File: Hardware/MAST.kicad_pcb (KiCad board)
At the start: 6 copper layers, 26 x 15 mm, 122 parts, among them J1 S+, J2 S-, J3 S-, J4 BAT+, J5 BAT-, Q1 DMP21D0UFB4, Q2 PMZ290UNE2, U1 LP5907SNX-3.0, U2 TPS62748, U3 ARTIC-R2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

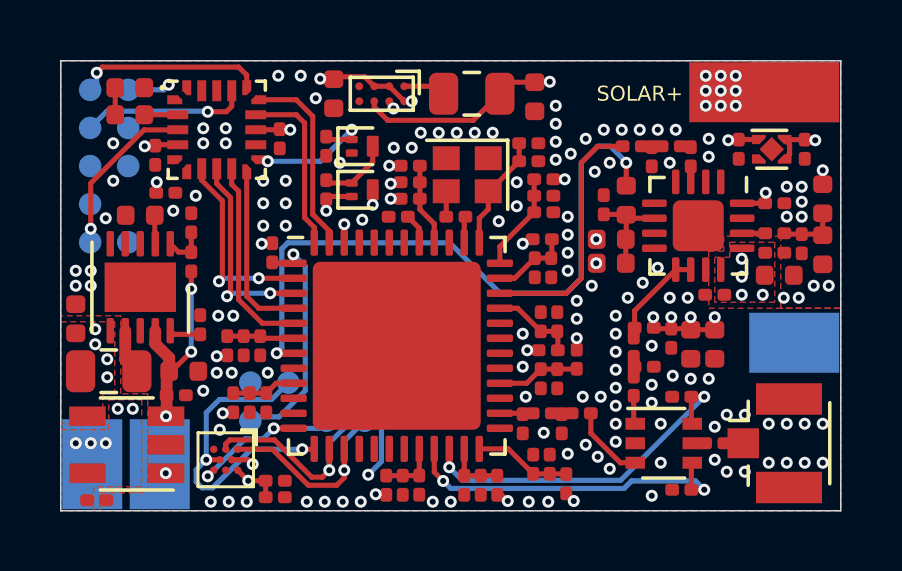
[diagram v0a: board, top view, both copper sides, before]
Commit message: Fix flash chip orientation
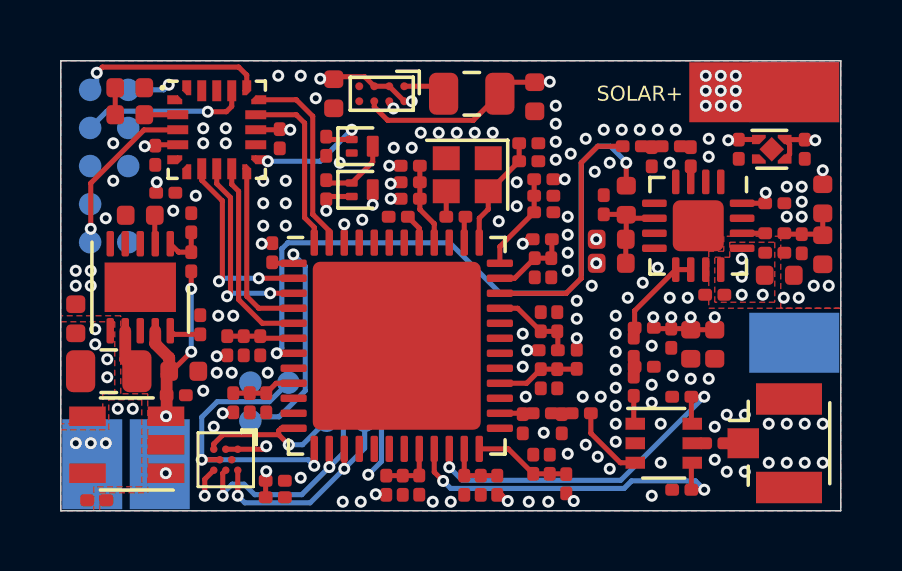
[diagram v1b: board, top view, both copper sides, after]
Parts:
- L1, L10, L2, L3, L4, L5, L6, L7, L8, L9: value 220@100MHz -> 120@100MHz
- R9: value 3.1M -> 3.09M
- X1: value 26MHz -> TCXO, 26MHz, <1ppm
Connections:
- U4 pad A1: FLASH_nEN -> ARTIC_3V3
- U4 pad A3: ARTIC_3V3 -> FLASH_nEN
- U4 pad C1: FLASH_MISO -> ARTIC_3V3
- U4 pad C3: Net-(U4-PadC3) -> FLASH_MISO
- U4 pad E1: Net-(U4-PadE1) -> FLASH_CLK
- U4 pad E3: FLASH_CLK -> ARTIC_3V3
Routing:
- net ARTIC_3V3: track 17.1 -> 18.7 mm, vias 16 -> 18
- net FLASH_MOSI: track 10.6 -> 9.78 mm
- net GND: track 1.74 -> 0.98 mm, vias 139 -> 134
- net FLASH_MISO: track 8.35 -> 9.02 mm, vias 1 -> 2
- net FLASH_CLK: track 5.67 -> 5.20 mm, vias 2 -> 1
- net FLASH_nEN: track 7.04 -> 7.51 mm, vias 1 -> 2

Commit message: Improve RF 1.8V & 3.3V rail power delivery
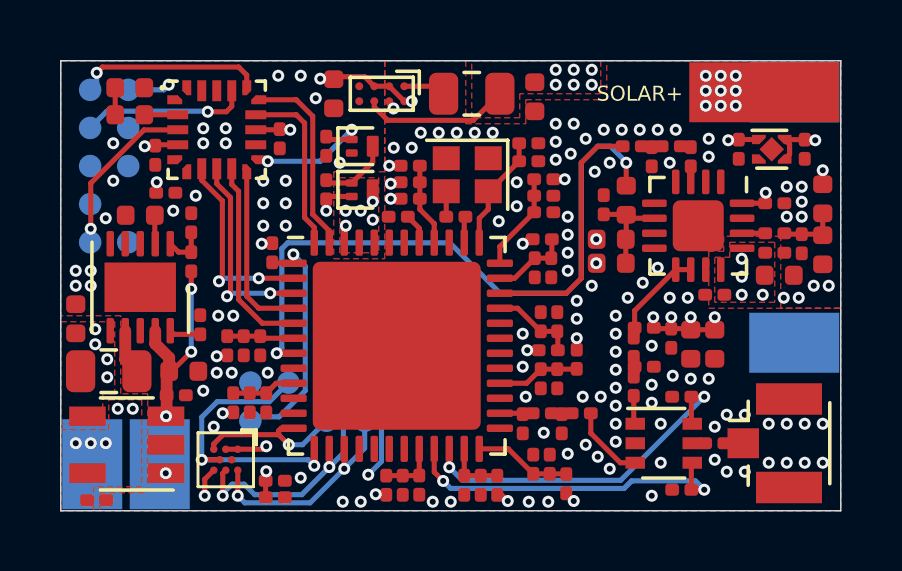
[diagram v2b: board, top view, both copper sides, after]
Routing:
- net ARTIC_1V8: track 9.37 -> 7.54 mm, vias 8 -> 13
- net ARTIC_3V3: track 18.7 -> 17.6 mm, vias 18 -> 21
- net GND: vias 134 -> 133
- added copper zone on F.Cu, net ARTIC_1V8
- added copper zone on F.Cu, net ARTIC_3V3
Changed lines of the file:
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@@
     (thickness 1.2)
     (drawings 12)
-    (tracks 574)
+    (tracks 575)
     (zones 0)
     (modules 122)
@@
   (via (at 207 45.6) (size 0.4) (drill 0.2) (layers F.Cu B.Cu) (net 1))
   (segment (start 207.33 45.6) (end 207 45.6) (width 0.171) (layer F.Cu) (net 1))
-  (via (at 206.05 46.3) (size 0.4) (drill 0.2) (layers F.Cu B.Cu) (net 1))
   (via (at 205.3 44.4) (size 0.4) (drill 0.2) (layers F.Cu B.Cu) (net 1))
   (via (at 201.7 51.4) (size 0.4) (drill 0.2) (layers F.Cu B.Cu) (net 1))
@@
   (segment (start 206.95 42.449772) (end 207.090137 42.589909) (width 0.171) (layer F.Cu) (net 1))
   (via (at 212.5 43.1) (size 0.4) (drill 0.2) (layers F.Cu B.Cu) (net 1))
-  (via (at 212.5 42.5) (size 0.4) (drill 0.2) (layers F.Cu B.Cu) (net 1))
   (via (at 202.75 45) (size 0.4) (drill 0.2) (layers F.Cu B.Cu) (net 1))
   (via (at 203.5 45) (size 0.4) (drill 0.2) (layers F.Cu B.Cu) (net 1))
@@
   (via (at 202.9 51.4) (size 0.4) (drill 0.2) (layers F.Cu B.Cu) (net 1))
   (via (at 201.1 53.2) (size 0.4) (drill 0.2) (layers F.Cu B.Cu) (net 1))
+  (via (at 213.1 43.1) (size 0.4) (drill 0.2) (layers F.Cu B.Cu) (net 1))
+  (via (at 206.4 45.7) (size 0.4) (drill 0.2) (layers F.Cu B.Cu) (net 9))
+  (via (at 205.5 46.5) (size 0.4) (drill 0.2) (layers F.Cu B.Cu) (net 9))
+  (via (at 206 46) (size 0.4) (drill 0.2) (layers F.Cu B.Cu) (net 9))
+  (via (at 205.5 46) (size 0.4) (drill 0.2) (layers F.Cu B.Cu) (net 9))
   (segment (start 218.75 53.75) (end 218.12 53.75) (width 0.171) (layer F.Cu) (net 2))
   (segment (start 212.57 50.04) (end 212.55 50.02) (width 0.171) (layer F.Cu) (net 3))
@@
   (via (at 212.8 44.95) (size 0.4) (drill 0.2) (layers F.Cu B.Cu) (net 9))
   (segment (start 212.42 44.95) (end 212.8 44.95) (width 0.171) (layer F.Cu) (net 9))
-  (via (at 205.45 46.45) (size 0.4) (drill 0.2) (layers F.Cu B.Cu) (net 9))
-  (segment (start 205.45 47.0625) (end 205.45 46.45) (width 0.171) (layer F.Cu) (net 9))
   (via (at 201.4 52.75) (size 0.4) (drill 0.2) (layers F.Cu B.Cu) (net 9))
   (segment (start 201.75 52.72) (end 201.43 52.72) (width 0.171) (layer F.Cu) (net 9))
@@
   (segment (start 206.13 51.73) (end 206.690501 52.290501) (width 0.171) (layer B.Cu) (net 9))
   (segment (start 206.690501 52.290501) (end 206.690501 54.359499) (width 0.171) (layer B.Cu) (net 9))
-  (via (at 206.4 45.8) (size 0.4) (drill 0.2) (layers F.Cu B.Cu) (net 9))
-  (segment (start 206.4 45.3) (end 206.4 45.8) (width 0.171) (layer F.Cu) (net 9))
   (via (at 210.9 55.675) (size 0.4) (drill 0.2) (layers F.Cu B.Cu) (net 9))
   (segment (start 210.55 55.47) (end 210.695 55.47) (width 0.171) (layer F.Cu) (net 9))
@@
   (via (at 202.85 54.6855) (size 0.4) (drill 0.2) (layers F.Cu B.Cu) (net 9))
   (segment (start 202.83 54.7055) (end 202.85 54.6855) (width 0.171) (layer F.Cu) (net 9))
+  (via (at 206.4 46.3) (size 0.4) (drill 0.2) (layers F.Cu B.Cu) (net 9))
   (via (at 218.25 43.65) (size 0.4) (drill 0.2) (layers F.Cu B.Cu) (net 10))
   (segment (start 218.6 43.63) (end 218.27 43.63) (width 0.171) (layer F.Cu) (net 10))
@@
   (segment (start 206.898127 42.98551) (end 206.45 42.537383) (width 0.171) (layer F.Cu) (net 15))
   (segment (start 210.6375 42.1) (end 209.75199 42.98551) (width 0.171) (layer F.Cu) (net 15))
-  (segment (start 211.0225 41.715) (end 210.6375 42.1) (width 0.171) (layer F.Cu) (net 15))
-  (segment (start 211.8 41.715) (end 211.0225 41.715) (width 0.171) (layer F.Cu) (net 15))
-  (segment (start 211.8 41.715) (end 212.285 41.715) (width 0.171) (layer F.Cu) (net 15))
-  (via (at 212.3 41.7) (size 0.4) (drill 0.2) (layers F.Cu B.Cu) (net 15))
-  (segment (start 212.285 41.715) (end 212.3 41.7) (width 0.171) (layer F.Cu) (net 15))
+  (via (at 212.5 41.8) (size 0.4) (drill 0.2) (layers F.Cu B.Cu) (net 15))
+  (via (at 212.5 41.3) (size 0.4) (drill 0.2) (layers F.Cu B.Cu) (net 15))
+  (via (at 213.1 41.3) (size 0.4) (drill 0.2) (layers F.Cu B.Cu) (net 15))
+  (via (at 213.1 41.8) (size 0.4) (drill 0.2) (layers F.Cu B.Cu) (net 15))
+  (via (at 213.7 41.8) (size 0.4) (drill 0.2) (layers F.Cu B.Cu) (net 15))
+  (via (at 213.7 41.3) (size 0.4) (drill 0.2) (layers F.Cu B.Cu) (net 15))
   (segment (start 211.28 43.75) (end 211.28 44.35) (width 0.171) (layer F.Cu) (net 16))
   (segment (start 210.28 45.35) (end 210.25 45.35) (width 0.171) (layer F.Cu) (net 16))
@@
       (pts
         (xy 197.3 56) (xy 197.3 55.4) (xy 198.9 55.4) (xy 198.9 52.1) (xy 198 52.1)
-        (xy 198 49.5) (xy 196 49.5) (xy 196 41) (xy 222 41) (xy 222 49.25)
-        (xy 220 49.25) (xy 220 46.85) (xy 218.1 46.85) (xy 218.1 47.35) (xy 217.6 47.35)
-        (xy 217.6 49.25) (xy 222 49.25) (xy 222 56)
+        (xy 198 49.5) (xy 196 49.5) (xy 196 41) (xy 206.8 41) (xy 206.8 44.7)
+        (xy 205.1 44.7) (xy 205.1 47.6) (xy 206.8 47.6) (xy 206.8 41) (xy 209.5 41)
+        (xy 209.5 43.1) (xy 211.5 43.1) (xy 211.5 42.3) (xy 214.2 42.3) (xy 214.2 41)
+        (xy 222 41) (xy 222 49.25) (xy 220 49.25) (xy 220 46.85) (xy 218.1 46.85)
+        (xy 218.1 47.35) (xy 217.6 47.35) (xy 217.6 49.25) (xy 222 49.25) (xy 222 56)
       )
     )
@@
       )
     )
+  )
+  (zone (net 15) (net_name ARTIC_1V8) (layer F.Cu) (hatch edge 0.508)
+    (connect_pads yes (clearance 0.1))
+    (min_thickness 0.1)
+    (fill yes (arc_segments 32) (thermal_gap 0.1) (thermal_bridge_width 0.2) (smoothing fillet) (radius 0.1))
+    (polygon
+      (pts
+        (xy 214 42.1) (xy 211.3 42.1) (xy 211.3 42.9) (xy 209.7 42.9) (xy 209.7 41)
+        (xy 214 41)
+      )
+    )
+  )
+  (zone (net 9) (net_name ARTIC_3V3) (layer F.Cu) (hatch edge 0.508)
+    (connect_pads yes (clearance 0.1))
+    (min_thickness 0.1)
+    (fill yes (arc_segments 32) (thermal_gap 0.1) (thermal_bridge_width 0.2) (smoothing fillet) (radius 0.1))
+    (polygon
+      (pts
+        (xy 206.6 47.4) (xy 205.3 47.4) (xy 205.3 44.9) (xy 206.6 44.9)
+      )
+    )

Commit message: Enable MPPC on solar charger
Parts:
- added R12: MPPC_SET, Resistor_SMD:R_0603_1608Metric, F.Cu at (196.7, 43.2)
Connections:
- U9 pad 5: GND -> Net-(R12-Pad1)
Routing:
- net Net-(R12-Pad1): track 0.00 -> 4.00 mm
- net GND: vias 133 -> 134
